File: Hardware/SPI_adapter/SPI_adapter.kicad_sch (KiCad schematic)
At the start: 5 parts, among them J1 Conn_02x07_Top_Bottom, J2 Conn_Coaxial, U1 RF-LORA-868-SO

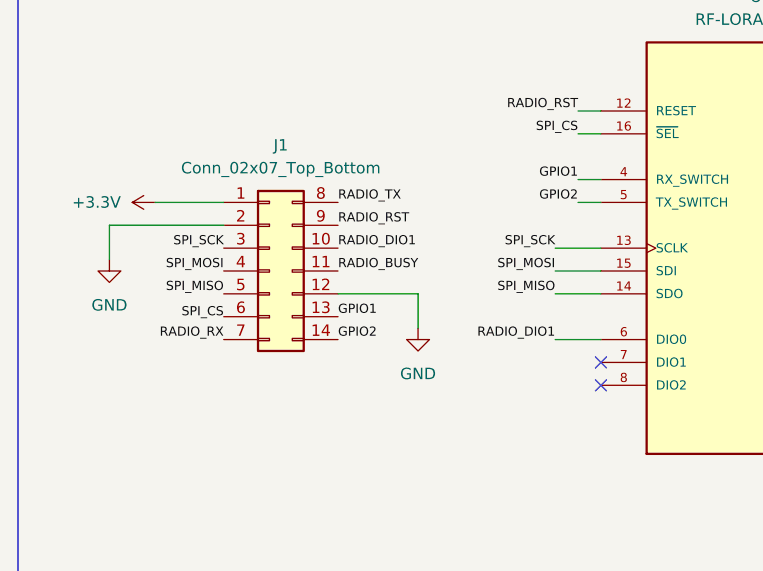
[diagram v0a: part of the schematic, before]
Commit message: Fixed USB traces, radio connectors, finished UART adapter
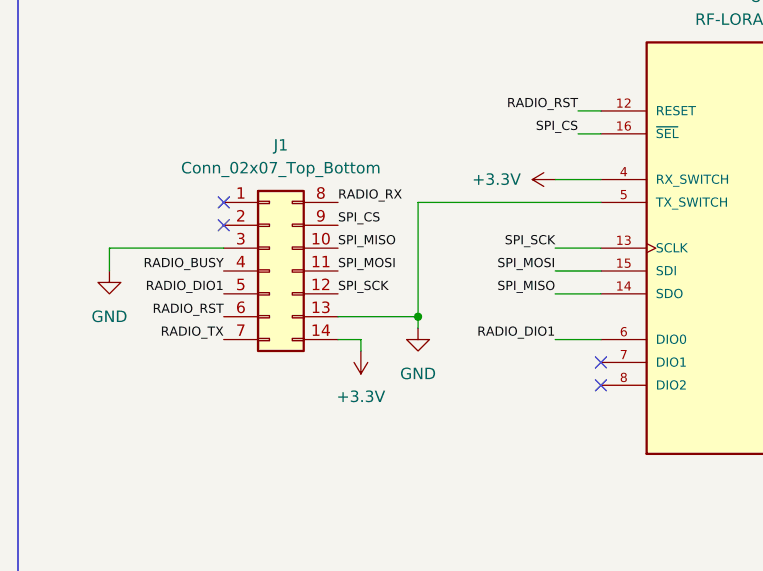
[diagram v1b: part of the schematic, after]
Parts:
- J2: footprint MHF4_antenna:TE_CONMHF4-SMD-G-T -> Connector_Coaxial:SMA_Molex_73251-1153_EdgeMount_Horizontal
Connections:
- net +3.3V: now also J1.14 (Pin_14), U1.4 (RX_SWITCH); no longer J1.1 (Pin_1)
- net GND: now also J1.13 (Pin_13), J1.3 (Pin_3), U1.5 (TX_SWITCH); no longer J1.12 (Pin_12), J1.2 (Pin_2)
- net RADIO_BUSY: now also J1.4 (Pin_4); no longer J1.11 (Pin_11)
- net RADIO_DIO1: now also J1.5 (Pin_5); no longer J1.10 (Pin_10)
- net RADIO_RST: now also J1.6 (Pin_6); no longer J1.9 (Pin_9)
- net RADIO_RX: now also J1.8 (Pin_8); no longer J1.7 (Pin_7)
- net RADIO_TX: now also J1.7 (Pin_7); no longer J1.8 (Pin_8)
- net SPI_CS: now also J1.9 (Pin_9)
- net SPI_MISO: now also J1.10 (Pin_10); no longer J1.5 (Pin_5)
- net SPI_MOSI: now also J1.11 (Pin_11); no longer J1.4 (Pin_4)
- net SPI_SCK: now also J1.12 (Pin_12); no longer J1.3 (Pin_3)
- removed net GPIO1: J1.13 (Pin_13), U1.4 (RX_SWITCH)
- removed net GPIO2: J1.14 (Pin_14), U1.5 (TX_SWITCH)
- no-connect marks 5 -> 7

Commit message: Fixed RF trace, Added new Diodes, better power traces and new switches
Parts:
- C2: footprint Capacitor_SMD:C_1210_3225Metric -> Capacitor_SMD:C_0805_2012Metric_Pad1.18x1.45mm_HandSolder
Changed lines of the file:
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@@
 			)
 		)
-		(property "Footprint" "Capacitor_SMD:C_1210_3225Metric"
+		(property "Footprint" "Capacitor_SMD:C_0805_2012Metric_Pad1.18x1.45mm_HandSolder"
 			(at 195.2752 88.9 0)
 			(effects

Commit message: SPI resistors removed and transmission added
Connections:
- net +3.3V: no longer U1.4 (RX_SWITCH)
- net GND: no longer U1.5 (TX_SWITCH)
- net RX_SWITCH: now reaches J1.1 (Pin_1)
- net RX_SWITCH: now also U1.4 (RX_SWITCH)
- net TX_SWITCH: now reaches J1.2 (Pin_2)
- net TX_SWITCH: now also U1.5 (TX_SWITCH)
- no-connect marks 7 -> 5
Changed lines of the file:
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@@
-		(color 0 0 0 0)
-	)
-	(junction
-		(at 116.84 102.87)
-		(diameter 0)
 		(color 0 0 0 0)
 	)
@@
 	)
 	(no_connect
-		(at 95.25 90.17)
-	)
-	(no_connect
 		(at 172.72 110.49)
 	)
@@
 	)
 	(no_connect
-		(at 95.25 92.71)
-	)
-	(no_connect
 		(at 137.16 110.49)
 	)
 	(wire
 		(pts
-			(xy 116.84 90.17) (xy 116.84 102.87)
-		)
-		(stroke
-			(width 0)
-			(type default)
-		)
-	)
-	(wire
-		(pts
 			(xy 181.61 81.28) (xy 187.96 81.28)
 		)
@@
 	(wire
 		(pts
+			(xy 92.71 92.71) (xy 95.25 92.71)
+		)
+		(stroke
+			(width 0)
+			(type default)
+		)
+	)
+	(wire
+		(pts
 			(xy 134.62 82.55) (xy 137.16 82.55)
 		)
@@
 	(wire
 		(pts
-			(xy 137.16 90.17) (xy 116.84 90.17)
-		)
-		(stroke
-			(width 0)
-			(type default)
-		)
-	)
-	(wire
-		(pts
 			(xy 187.96 74.93) (xy 194.31 74.93)
+		)
+		(stroke
+			(width 0)
+			(type default)
+		)
+	)
+	(wire
+		(pts
+			(xy 92.71 90.17) (xy 95.25 90.17)
 		)
 		(stroke
@@
 		)
 	)
+	(label "RX_SWITCH"
+		(at 132.08 87.63 180)
+		(effects
+			(font
+				(size 1.27 1.27)
+			)
+			(justify right bottom)
+		)
+	)
 	(label "SPI_MOSI"
 		(at 132.08 97.79 180)
@@
 		)
 	)
+	(label "RX_SWITCH"
+		(at 92.71 90.17 180)
+		(effects
+			(font
+				(size 1.27 1.27)
+			)
+			(justify right bottom)
+		)
+	)
+	(label "TX_SWITCH"
+		(at 92.71 92.71 180)
+		(effects
+			(font
+				(size 1.27 1.27)
+			)
+			(justify right bottom)
+		)
+	)
 	(label "RADIO_DIO1"
 		(at 95.25 100.33 180)
@@
 			)
 			(justify left bottom)
+		)
+	)
+	(label "TX_SWITCH"
+		(at 137.16 90.17 180)
+		(effects
+			(font
+				(size 1.27 1.27)
+			)
+			(justify right bottom)
 		)
 	)
@@
 					(unit 1)
 				)
-			)
-		)
-	)
-	(symbol
-		(lib_id "power:+3.3V")
-		(at 132.08 87.63 90)
-		(unit 1)
-		(exclude_from_sim no)
-		(in_bom yes)
-		(on_board yes)
-		(dnp no)
-		(fields_autoplaced yes)
-		(property "Reference" "#PWR08"
-			(at 135.89 87.63 0)
-			(effects
-				(font
-					(size 1.27 1.27)
-				)
-				(hide yes)
-			)
-		)
-		(property "Value" "+3.3V"
-			(at 128.27 87.6299 90)
-			(effects
-				(font
-					(size 1.27 1.27)
-				)
-				(justify left)
-			)
-		)
-		(property "Footprint" ""
-			(at 132.08 87.63 0)
-			(effects
-				(font
-					(size 1.27 1.27)
-				)
-				(hide yes)
-			)
-		)
-		(property "Datasheet" ""
-			(at 132.08 87.63 0)
-			(effects
-				(font
-					(size 1.27 1.27)
-				)
-				(hide yes)
-			)
-		)
-		(property "Description" "Power symbol creates a global label with name \"+3.3V\""
-			(at 132.08 87.63 0)
-			(effects
-				(font
-					(size 1.27 1.27)
-				)
-				(hide yes)
-			)
-		)
-		(pin "1"
-		)
-		(instances
-			(project "SPI_adapter"
-				(path "/dd2a81cc-f429-440b-88d8-e89075ace122"
-					(reference "#PWR08")
-					(unit 1)
-				)
